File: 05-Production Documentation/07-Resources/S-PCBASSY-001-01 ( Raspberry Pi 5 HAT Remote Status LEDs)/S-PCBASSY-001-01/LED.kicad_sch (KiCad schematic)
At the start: 0 parts

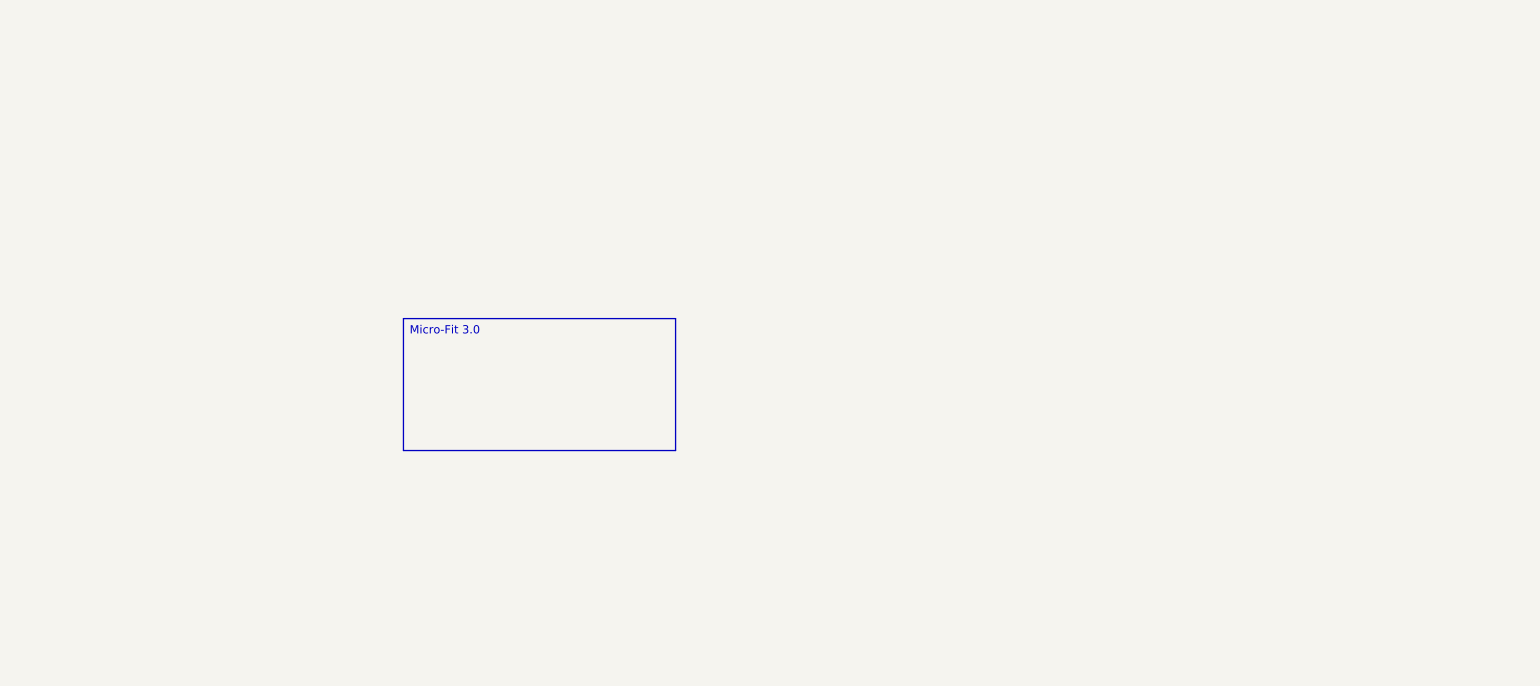
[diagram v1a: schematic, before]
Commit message: Connector added with TVS still need to add polarity Protection
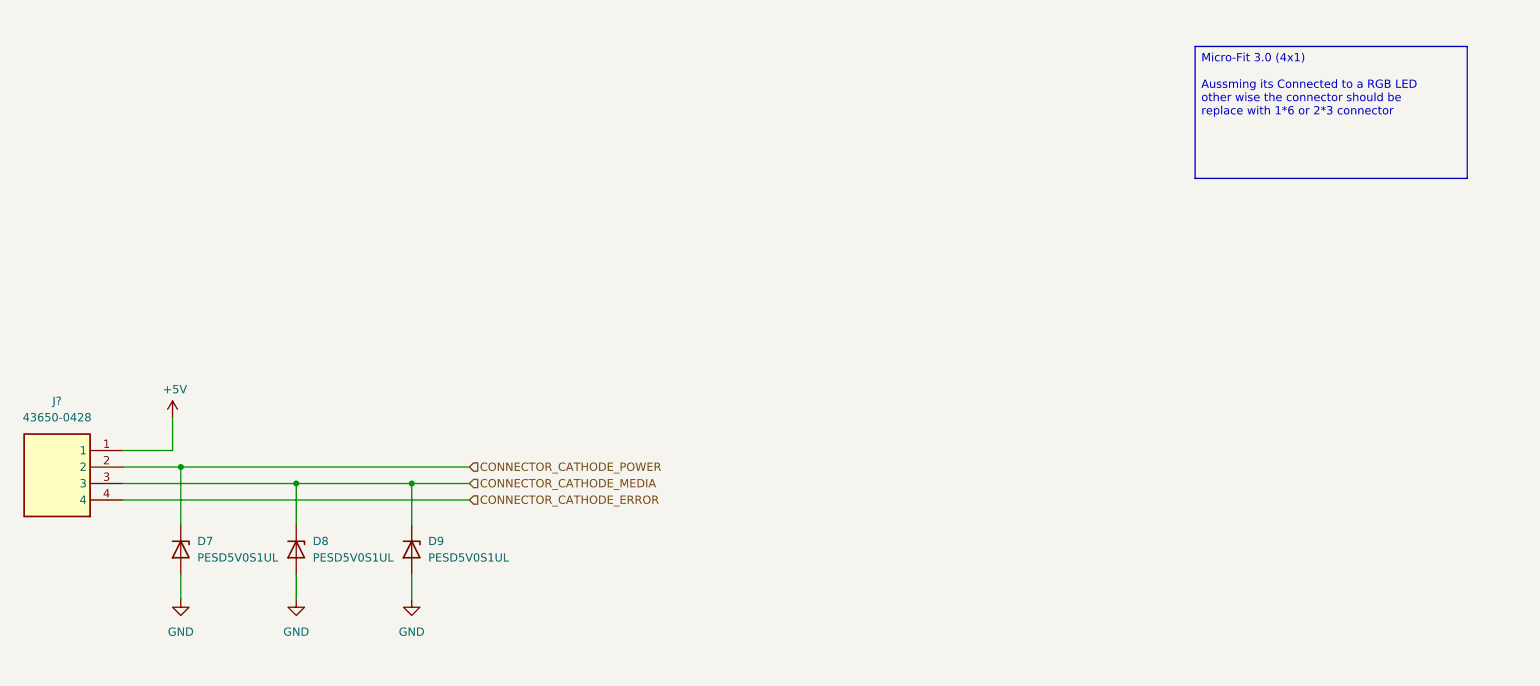
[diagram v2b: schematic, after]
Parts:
- added D7, D8, D9: PESD5V0S1UL, Diode_SMD:D_SOD-882, symbol Diode:PESD5V0S1UL
- added J?: 43650-0428, Connector:43650-04YY_272829, symbol Connector:43650-0428
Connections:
- new net +5V: J?.1
- new net CONNECTOR_CATHODE_ERROR: J?.4
- new net CONNECTOR_CATHODE_MEDIA: D8.1 (K), D9.1 (K), J?.3
- new net CONNECTOR_CATHODE_POWER: D7.1 (K), J?.2
- new net GND: D7.2 (A), D8.2 (A), D9.2 (A)

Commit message: Schematics done
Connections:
- net CONNECTOR_CATHODE_ERROR: now also D9.1 (K)
- net CONNECTOR_CATHODE_MEDIA: no longer D9.1 (K)
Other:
- note added: "Notes"
- note added: "RGB Molex Connector"
- moved on the sheet: D7, D8, D9, J?

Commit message: ERC Completed and passed
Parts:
- gave numbers to parts that had none: 1
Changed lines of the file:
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@@
 		(dnp no)
 		(fields_autoplaced yes)
-		(property "Reference" "J?"
+		(property "Reference" "J2"
 			(at 107.95 74.93 0)
 			(effects
@@
 			(project "S-PCBASSY-001-01"
 				(path "/e63e39d7-6ac0-4ffd-8aa3-1841a4541b55/dd804605-115d-4be8-9c67-9010d8abb097"
-					(reference "J?")
+					(reference "J2")
 					(unit 1)
 				)

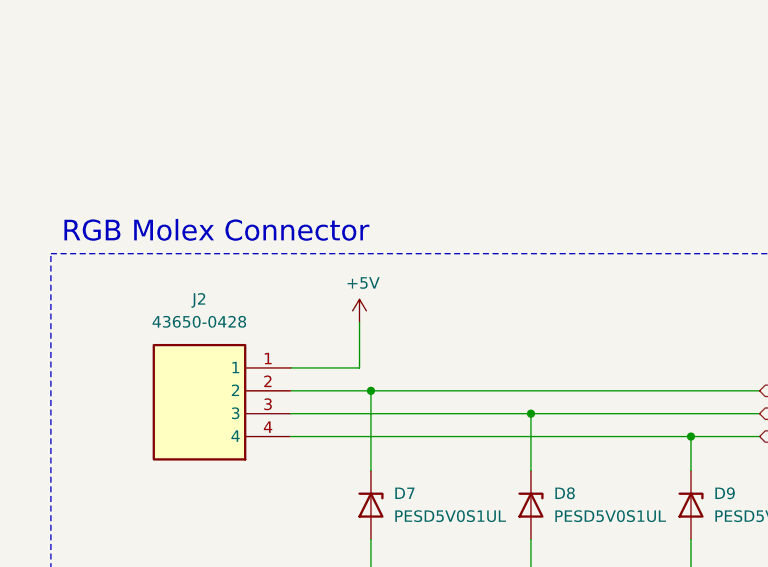
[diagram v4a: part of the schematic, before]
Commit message: PCB Routing done
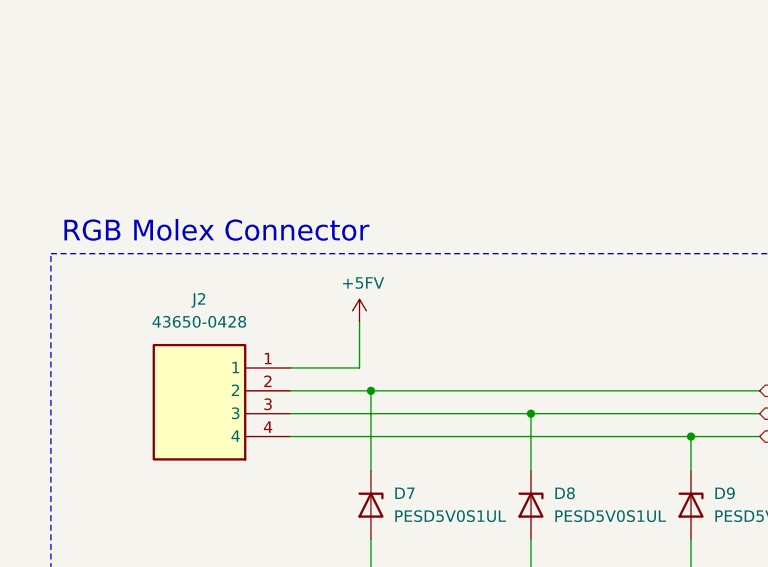
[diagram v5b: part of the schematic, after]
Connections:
- net +5V renamed +5FV
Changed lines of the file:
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@@
 			)
 		)
-		(property "Value" "+5V"
+		(property "Value" "+5FV"
 			(at 126.0983 73.1456 0)
 			(effects
